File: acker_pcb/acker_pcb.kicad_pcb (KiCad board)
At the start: 2 copper layers, 7 parts, among them J1 XT60, J2 servo_header, J3 DC barrel jack, U1 Buck_Module, U2 Buck_Module, U3 dc_motor_controller

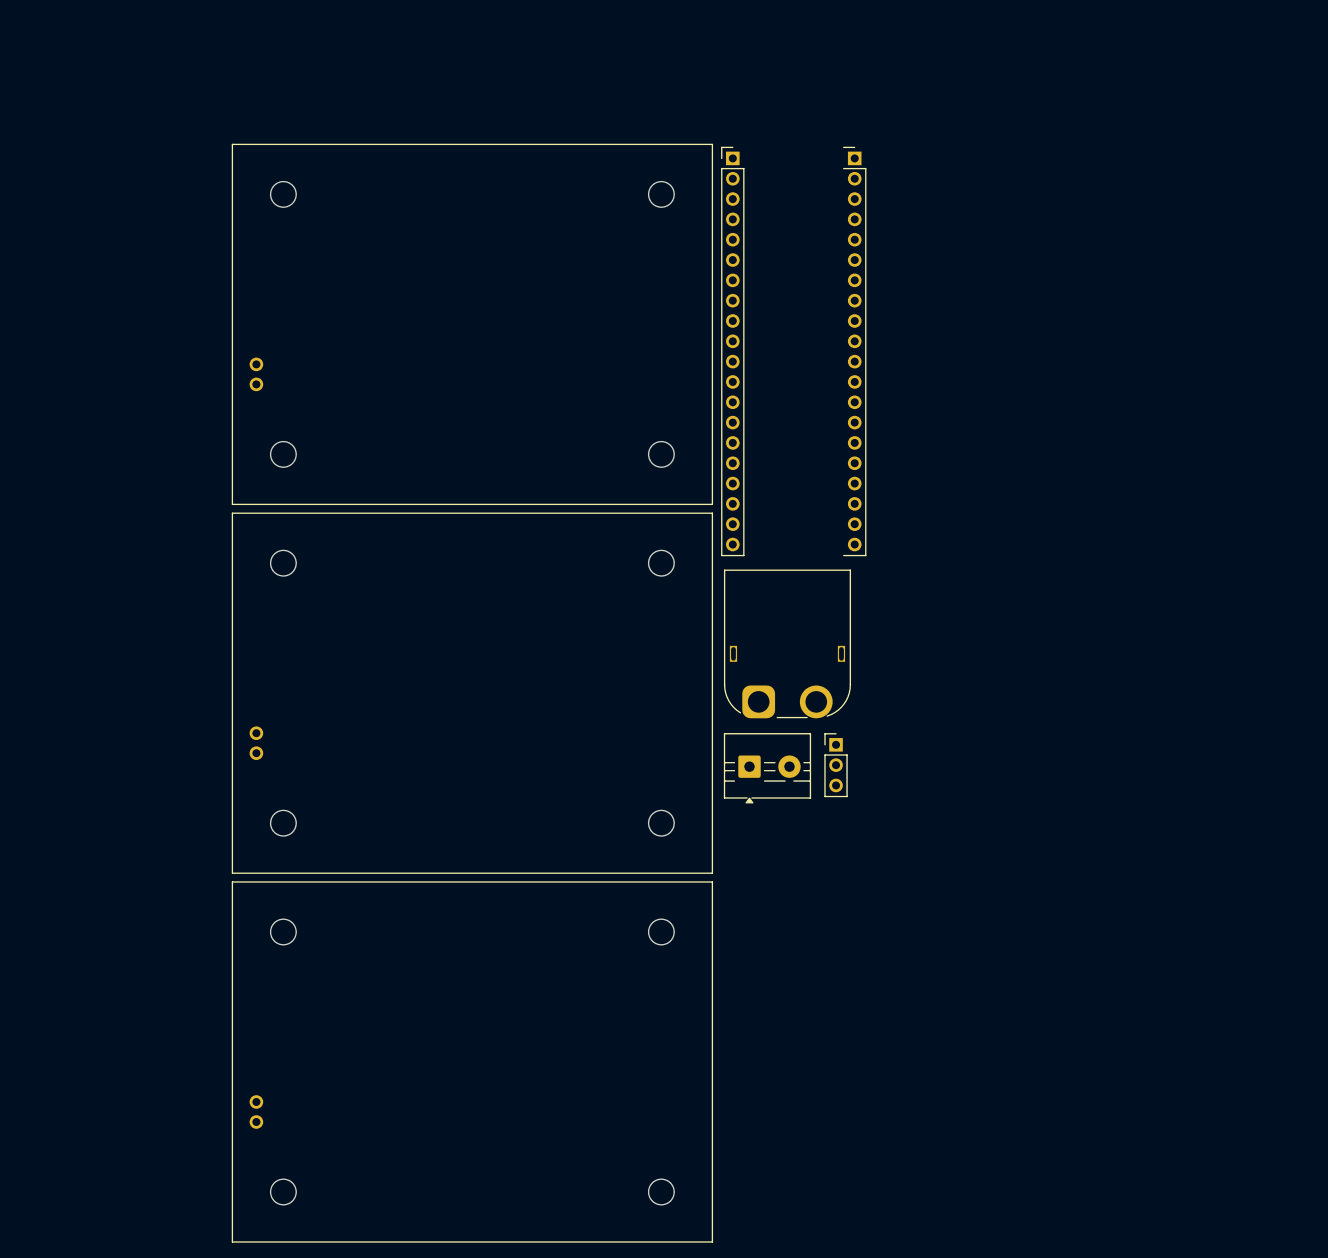
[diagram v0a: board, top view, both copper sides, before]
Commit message: corrected the switch
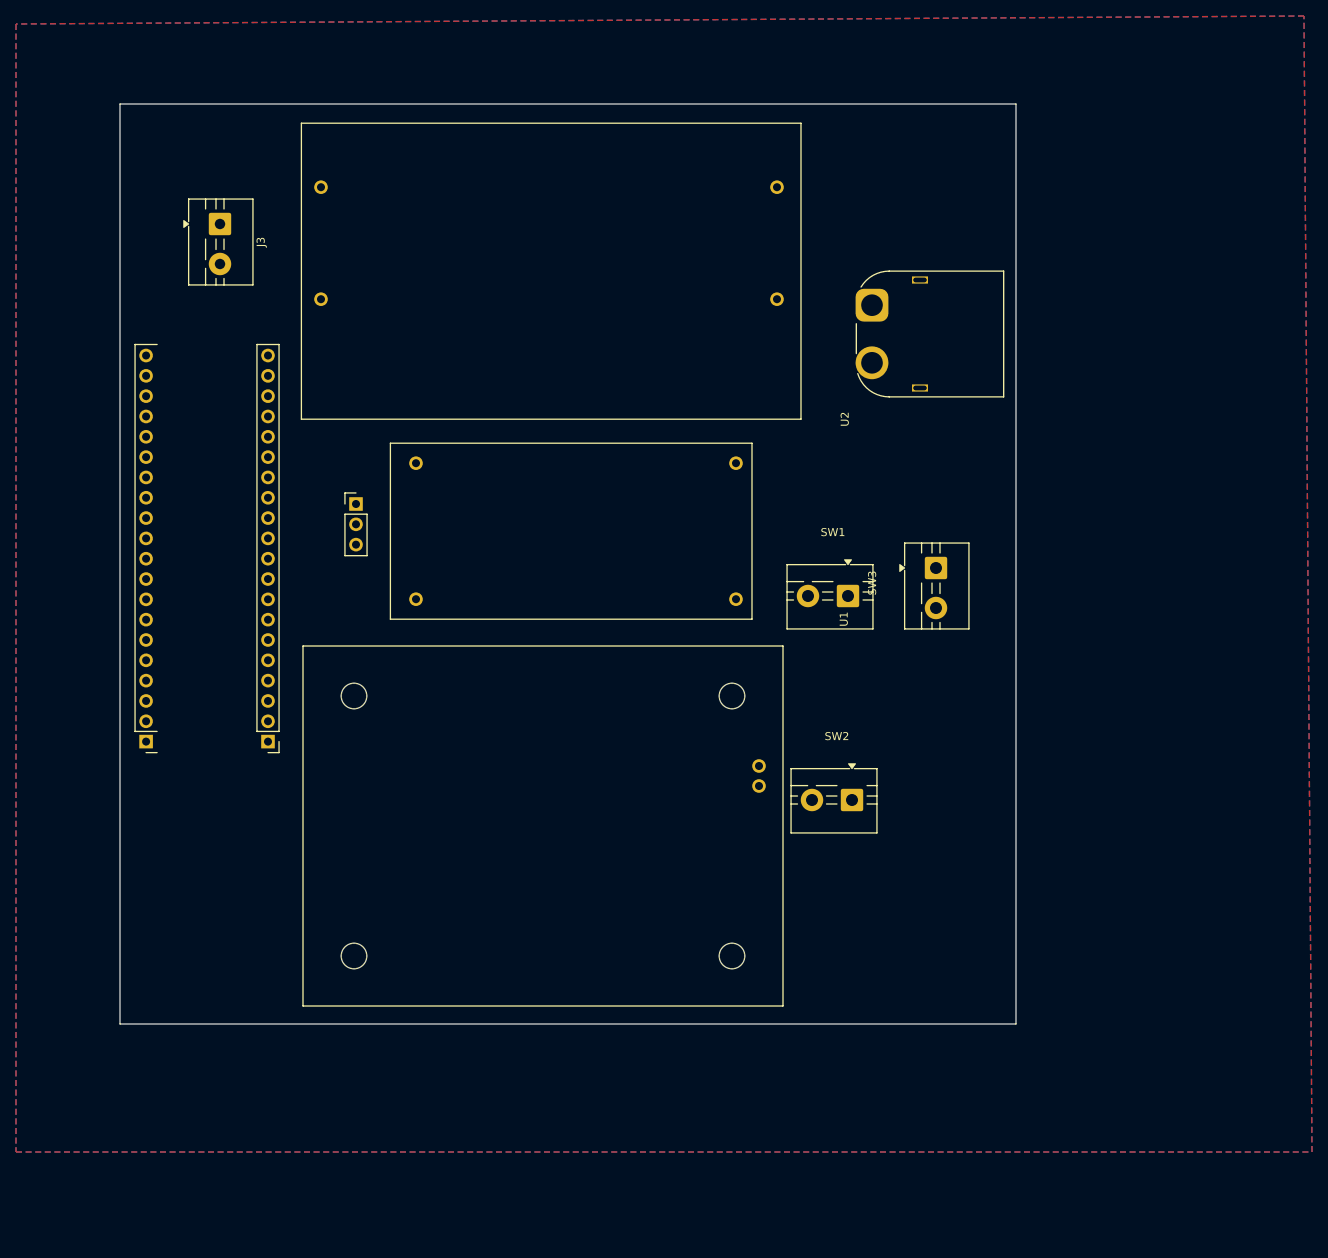
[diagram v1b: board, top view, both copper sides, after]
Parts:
- added SW1: SW_SPST, acker_chassis:spst_switch, F.Cu at (163.0, 97.5)
- added SW2: SW_SPST, acker_chassis:spst_switch, F.Cu at (163.5, 123.0)
- added SW3: SW_SPST, acker_chassis:spst_switch, F.Cu at (174.0, 94.0)
- U1: footprint acker_chassis:YX-4055AM motor drive chip -> acker_chassis:XL4015 Buck
- U2: footprint acker_chassis:YX-4055AM motor drive chip -> acker_chassis:XL4016 BUCK
- moved J3 94.8 mm to (84.5, 51.0), turned to -90 degrees
- moved μC1 93.2 mm to (90.5, 115.7), turned to 180 degrees
- moved J2 67.1 mm to (101.5, 86.0)
- moved U2 53.5 mm to (157.1, 75.4), turned to 90 degrees
- moved J1 51.6 mm to (166.0, 61.1), turned to -90 degrees
- moved U1 50.8 mm to (151.0, 100.4), turned to 90 degrees
- moved U3 30.8 mm to (124.9, 126.2), turned to 180 degrees
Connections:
- J3 pad 1: GND -> Net-(J3-Pin_1)
- J3 pad 2: Net-(J3-Pin_2) -> GND
- U1 pad 1: +12V -> Net-(SW1-B)
- U2 pad 1: +12V -> GND
- U2 pad 2: GND -> Net-(SW1-A)
- U3 pad 1: +12V -> Net-(SW2-B)
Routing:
- added copper zone on B.Cu, net GND
- added copper zone on F.Cu, net GND
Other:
- board outline added: 112 x 115 mm

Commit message: final design
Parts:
- moved SW3 11.0 mm to (173.2, 83.1), turned to 0 degrees
- renumbered SW2 to SW_motor, SW1 to SW_servo
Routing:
- net Net-(SW1-A): track 0.00 -> 103.6 mm
- net +12V: track 0.00 -> 17.7 mm
- net Net-(J3-Pin_1): track 0.00 -> 14.5 mm
- net Net-(J2-signal): track 0.00 -> 13.8 mm
- net Net-(J2-servo_power): track 0.00 -> 12.5 mm
- net Net-(SW1-B): track 0.00 -> 9.17 mm
- net Net-(SW2-B): track 0.00 -> 7.35 mm

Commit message: final design
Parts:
- added REF**: MountingHole_3mm, MountingHole:MountingHole_3mm, F.Cu at (140.0, 117.5)
- added REF**: MountingHole_3mm, MountingHole:MountingHole_3mm, F.Cu at (140.0, 134.0)
- added REF**: MountingHole_3mm, MountingHole:MountingHole_3mm, F.Cu at (176.0, 41.0)
- added REF**: MountingHole_3mm, MountingHole:MountingHole_3mm, F.Cu at (108.0, 134.0)
- added REF**: MountingHole_3mm, MountingHole:MountingHole_3mm, F.Cu at (108.0, 117.5)
- added REF**: MountingHole_3mm, MountingHole:MountingHole_3mm, F.Cu at (80.0, 41.0)
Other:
- board text added: "Blackpill"
